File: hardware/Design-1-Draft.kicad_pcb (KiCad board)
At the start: 2 copper layers, 125 x 180 mm, 37 parts, among them J1 Barrel_Jack_Switch, M1 WATERPUMP-1, M2 WATERPUMP-2, Q1 IRLZ44N, Q2 IRLZ44N, Q3 PN2222A, SW1 Button, U3 ADS1115, U5 Tang_Nano_9K

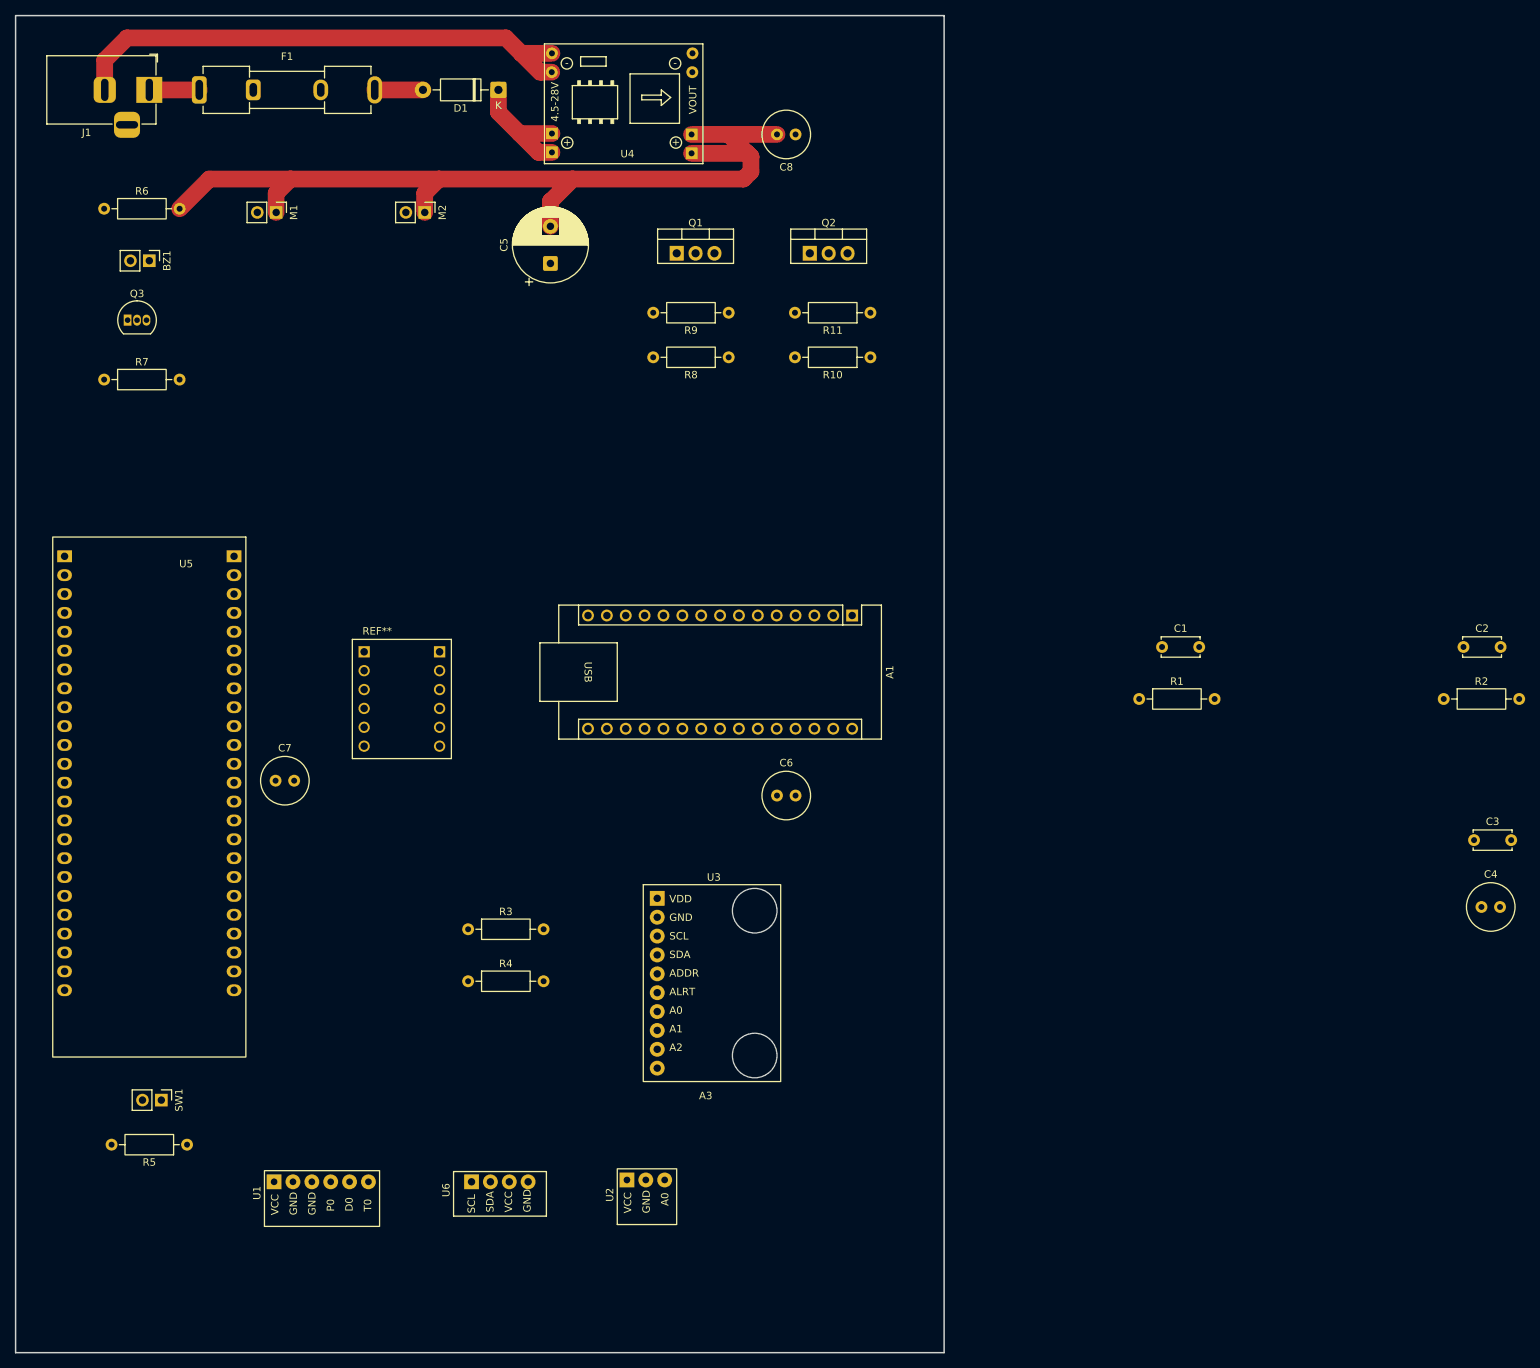
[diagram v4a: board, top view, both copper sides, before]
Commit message: updated schem (added multiple caps & 2 flyback diodes @pumps)
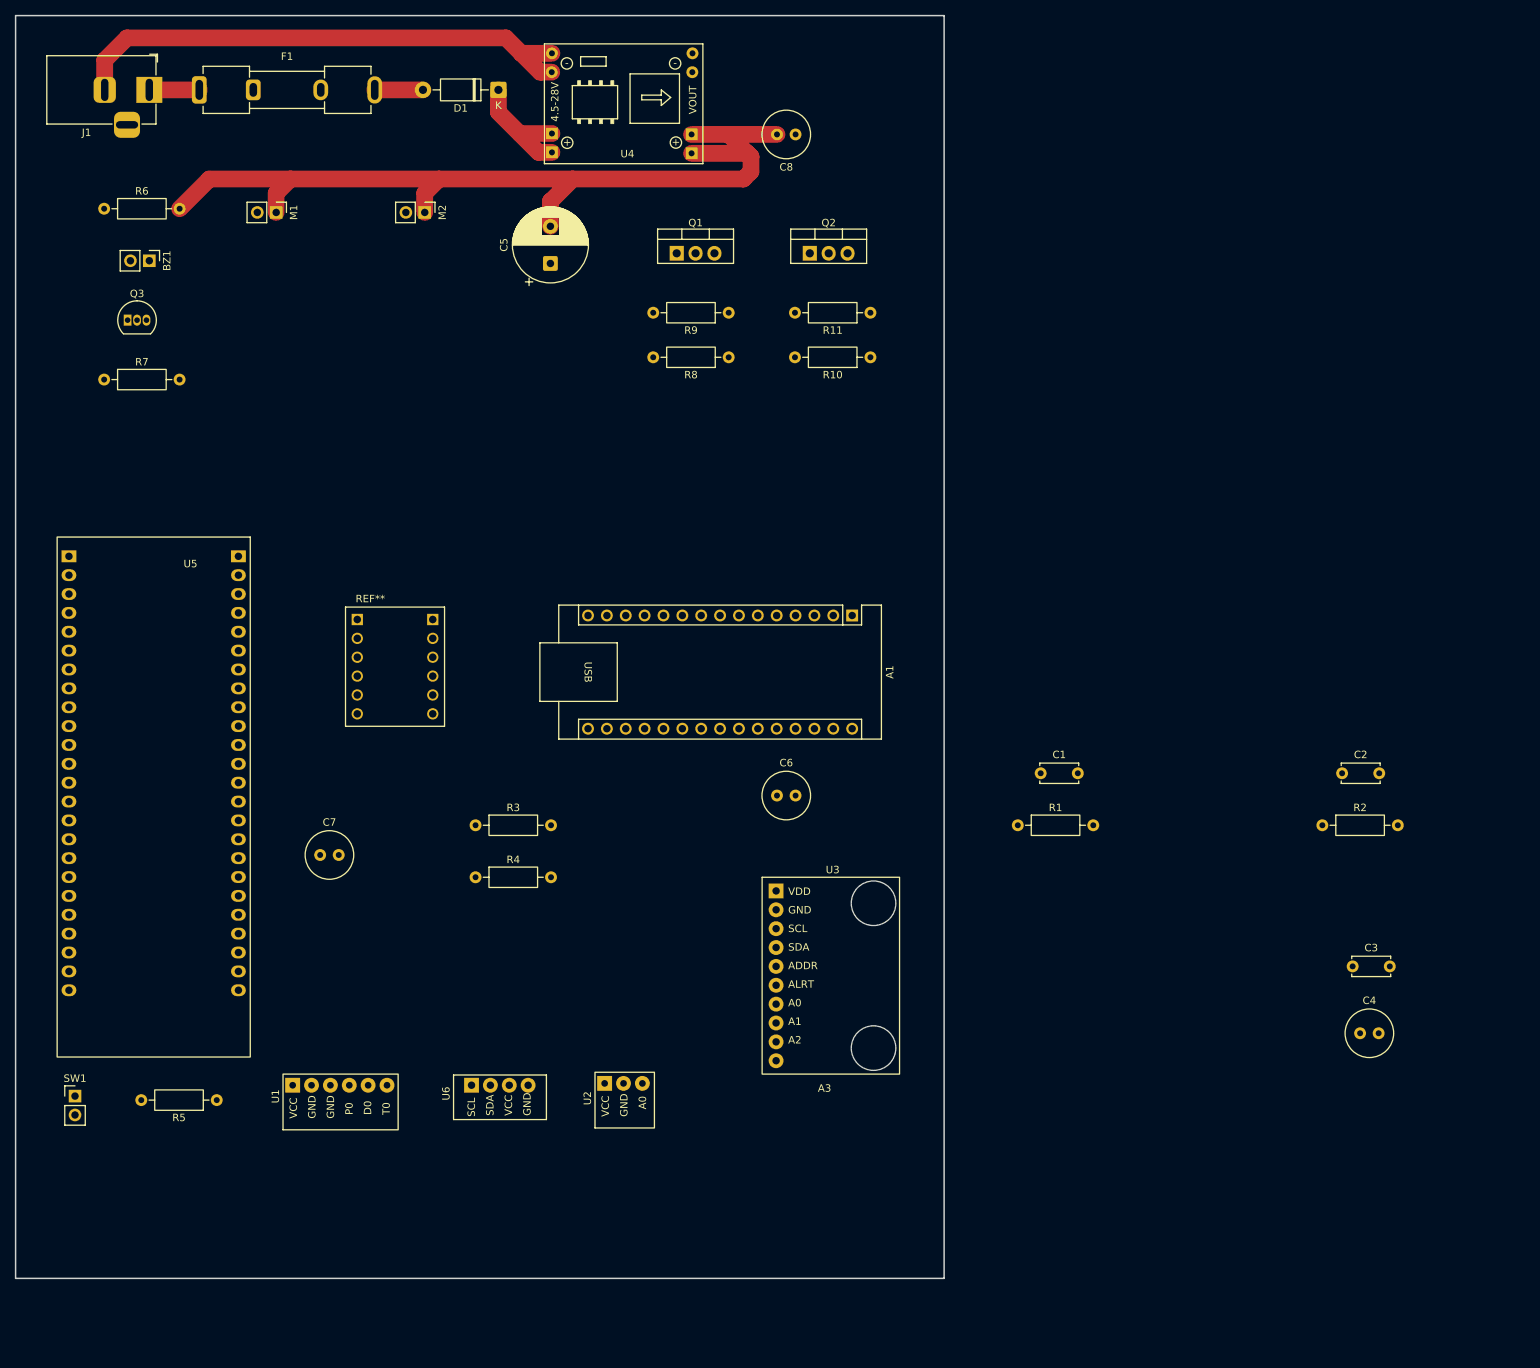
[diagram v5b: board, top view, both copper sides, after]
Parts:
- moved C1 23.6 mm to (162.0, 117.0)
- moved C3 23.6 mm to (204.0, 143.0)
- moved C4 23.6 mm to (205.0, 152.0)
- moved R1 23.6 mm to (158.9, 124.0)
- moved R2 23.6 mm to (199.9, 124.0)
- moved C2 23.6 mm to (202.6, 117.0)
- moved U3 16.0 mm to (134.0, 143.0)
- moved R3 14.0 mm to (85.9, 124.0)
- moved R4 14.0 mm to (85.9, 131.0)
- moved U2 13.3 mm to (106.0, 161.0)
- moved U1 13.2 mm to (67.5, 161.0)
- moved U6 13.0 mm to (89.2, 160.5)
- moved C7 11.7 mm to (65.0, 128.0)
- moved SW1 11.6 mm to (32.0, 160.5), turned to 0 degrees
- moved R5 7.21 mm to (51.1, 161.0)
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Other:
- board size 125 x 180 mm -> 125 x 170 mm
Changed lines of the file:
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@@
 	(footprint "Resistor_THT:R_Axial_DIN0207_L6.3mm_D2.5mm_P10.16mm_Horizontal"
 		(layer "F.Cu")
-		(at 84.92 145)
+		(at 85.92 131)
 		(descr "Resistor, Axial_DIN0207 series, Axial, Horizontal, pin pitch=10.16mm, 0.25W = 1/4W, length*diameter=6.3*2.5mm^2, http://cdn-reichelt.de/documents/datenblatt/B400/1_4W%23YAG.pdf")
 		(tags "Resistor Axial_DIN0207 series Axial Horizontal pin pitch 10.16mm 0.25W = 1/4W length 6.3mm diameter 2.5mm")
@@
 	(footprint "Resistor_THT:R_Axial_DIN0207_L6.3mm_D2.5mm_P10.16mm_Horizontal"
 		(layer "F.Cu")
-		(at 84.92 138)
+		(at 85.92 124)
 		(descr "Resistor, Axial_DIN0207 series, Axial, Horizontal, pin pitch=10.16mm, 0.25W = 1/4W, length*diameter=6.3*2.5mm^2, http://cdn-reichelt.de/documents/datenblatt/B400/1_4W%23YAG.pdf")
 		(tags "Resistor Axial_DIN0207 series Axial Horizontal pin pitch 10.16mm 0.25W = 1/4W length 6.3mm diameter 2.5mm")
@@
 	(footprint "Capacitor_THT:C_Radial_D6.3mm_H5.0mm_P2.50mm"
 		(layer "F.Cu")
-		(at 221.34 135)
+		(at 205 152)
 		(descr "C, Radial series, Radial, pin pitch=2.50mm, diameter=6.3mm, height=5mm, Non-Polar Electrolytic Capacitor")
 		(tags "C Radial series Radial pin pitch 2.50mm diameter 6.3mm height 5mm Non-Polar Electrolytic Capacitor")
@@
 	(footprint "1_CustomFootprints:TDS-ANALOG-SENSOR"
 		(layer "F.Cu")
-		(at 109 174 90)
+		(at 106 161 90)
 		(property "Reference" "U2"
 			(at 0.25 -5 90)
@@
 	(footprint "Resistor_THT:R_Axial_DIN0207_L6.3mm_D2.5mm_P10.16mm_Horizontal"
 		(layer "F.Cu")
-		(at 216.26 107)
+		(at 199.92 124)
 		(descr "Resistor, Axial_DIN0207 series, Axial, Horizontal, pin pitch=10.16mm, 0.25W = 1/4W, length*diameter=6.3*2.5mm^2, http://cdn-reichelt.de/documents/datenblatt/B400/1_4W%23YAG.pdf")
 		(tags "Resistor Axial_DIN0207 series Axial Horizontal pin pitch 10.16mm 0.25W = 1/4W length 6.3mm diameter 2.5mm")
@@
 	(footprint "1_CustomFootprints:CONV_BOB-12009"
 		(layer "F.Cu")
-		(at 76 107)
+		(at 75.08 102.65)
 		(property "Reference" "REF**"
 			(at -3.325 -9.135 0)
@@
 	(footprint "1_CustomFootprints:PH-4502C"
 		(layer "F.Cu")
-		(at 65 174 90)
+		(at 67.5 161 90)
 		(property "Reference" "U1"
 			(at 0.5 -8.5 90)
@@
 	(footprint "1_CustomFootprints:ADS1115"
 		(layer "F.Cu")
-		(at 118 144)
+		(at 134 143)
 		(property "Reference" "U3"
 			(at 0 -13 0)
@@
 	(footprint "Capacitor_THT:C_Disc_D5.0mm_W2.5mm_P5.00mm"
 		(layer "F.Cu")
-		(at 178.34 100)
+		(at 162 117)
 		(descr "C, Disc series, Radial, pin pitch=5.00mm, diameter*width=5*2.5mm^2, Capacitor, http://cdn-reichelt.de/documents/datenblatt/B300/DS_KERKO_TC.pdf")
 		(tags "C Disc series Radial pin pitch 5.00mm diameter 5mm width 2.5mm Capacitor")
@@
 	(footprint "Capacitor_THT:C_Radial_D6.3mm_H5.0mm_P2.50mm"
 		(layer "F.Cu")
-		(at 59 118)
+		(at 65 128)
 		(descr "C, Radial series, Radial, pin pitch=2.50mm, diameter=6.3mm, height=5mm, Non-Polar Electrolytic Capacitor")
 		(tags "C Radial series Radial pin pitch 2.50mm diameter 6.3mm height 5mm Non-Polar Electrolytic Capacitor")
@@
 	(footprint "Connector_PinHeader_2.54mm:PinHeader_1x02_P2.54mm_Vertical"
 		(layer "F.Cu")
-		(at 43.62 161 -90)
+		(at 32 160.46)
 		(descr "Through hole straight pin header, 1x02, 2.54mm pitch, single row")
 		(tags "Through hole pin header THT 1x02 2.54mm single row")
 		(property "Reference" "SW1"
-			(at 0 -2.38 90)
+			(at 0 -2.38 0)
 			(layer "F.SilkS")
 			(effects
@@
 		)
 		(property "Value" "Button"
-			(at 0 4.92 90)
+			(at 0 4.92 0)
 			(layer "F.Fab")
 			(effects
@@
 		)
 		(property "Datasheet" "~"
-			(at 0 0 90)
+			(at 0 0 0)
 			(layer "F.Fab")
 			(hide yes)
@@
 		)
 		(property "Description" "Push button switch, generic, two pins"
-			(at 0 0 90)
+			(at 0 0 0)
 			(layer "F.Fab")
 			(hide yes)
@@
 		(attr through_hole)
 		(fp_line
-			(start -1.38 3.92)
-			(end 1.38 3.92)
+			(start -1.38 -1.38)
+			(end 0 -1.38)
 			(stroke
 				(width 0.12)
@@
 		)
 		(fp_line
-			(start -1.38 1.27)
-			(end -1.38 3.92)
+			(start -1.38 0)
+			(end -1.38 -1.38)
 			(stroke
 				(width 0.12)
@@
 		(fp_line
 			(start -1.38 1.27)
-			(end 1.38 1.27)
+			(end -1.38 3.92)
 			(stroke
 				(width 0.12)
@@
 		)
 		(fp_line
-			(start 1.38 1.27)
-			(end 1.38 3.92)
+			(start -1.38 1.27)
+			(end 1.38 1.27)
 			(stroke
 				(width 0.12)
@@
 		)
 		(fp_line
-			(start -1.38 0)
-			(end -1.38 -1.38)
+			(start -1.38 3.92)
+			(end 1.38 3.92)
 			(stroke
 				(width 0.12)
@@
 		)
 		(fp_line
-			(start -1.38 -1.38)
-			(end 0 -1.38)
+			(start 1.38 1.27)
+			(end 1.38 3.92)
 			(stroke
 				(width 0.12)
@@
 		)
 		(fp_line
-			(start -1.77 4.32)
-			(end 1.77 4.32)
+			(start -1.77 -1.77)
+			(end -1.77 4.32)
 			(stroke
 				(width 0.05)
@@
 		)
 		(fp_line
-			(start 1.77 4.32)
-			(end 1.77 -1.77)
+			(start -1.77 4.32)
+			(end 1.77 4.32)
 			(stroke
 				(width 0.05)
@@
 		)
 		(fp_line
-			(start -1.77 -1.77)
-			(end -1.77 4.32)
+			(start 1.77 -1.77)
+			(end -1.77 -1.77)
 			(stroke
 				(width 0.05)
@@
 		)
 		(fp_line
-			(start 1.77 -1.77)
-			(end -1.77 -1.77)
+			(start 1.77 4.32)
+			(end 1.77 -1.77)
 			(stroke
 				(width 0.05)
@@
 		)
 		(fp_line
-			(start -1.27 3.81)
-			(end -1.27 -0.635)
+			(start -1.27 -0.635)
+			(end -0.635 -1.27)
 			(stroke
 				(width 0.1)
@@
 		)
 		(fp_line
-			(start 1.27 3.81)
-			(end -1.27 3.81)
+			(start -1.27 3.81)
+			(end -1.27 -0.635)
 			(stroke
 				(width 0.1)
@@
 		)
 		(fp_line
-			(start -1.27 -0.635)
-			(end -0.635 -1.27)
+			(start -0.635 -1.27)
+			(end 1.27 -1.27)
 			(stroke
 				(width 0.1)
@@
 		)
 		(fp_line
-			(start -0.635 -1.27)
-			(end 1.27 -1.27)
+			(start 1.27 -1.27)
+			(end 1.27 3.81)
 			(stroke
 				(width 0.1)
@@
 		)
 		(fp_line
-			(start 1.27 -1.27)
-			(end 1.27 3.81)
+			(start 1.27 3.81)
+			(end -1.27 3.81)
 			(stroke
 				(width 0.1)
@@
 		)
 		(fp_text user "${REFERENCE}"
-			(at 0 1.27 0)
+			(at 0 1.27 90)
 			(layer "F.Fab")
 			(effects
@@
 		)
 		(pad "1" thru_hole rect
-			(at 0 0 270)
+			(at 0 0)
 			(size 1.7 1.7)
 			(drill 1)
@@
 		)
 		(pad "2" thru_hole circle
-			(at 0 2.54 270)
+			(at 0 2.54)
 			(size 1.7 1.7)
 			(drill 1)
@@
 	(footprint "Capacitor_THT:C_Disc_D5.0mm_W2.5mm_P5.00mm"
 		(layer "F.Cu")
-		(at 220.34 126)
+		(at 204 143)
 		(descr "C, Disc series, Radial, pin pitch=5.00mm, diameter*width=5*2.5mm^2, Capacitor, http://cdn-reichelt.de/documents/datenblatt/B300/DS_KERKO_TC.pdf")
 		(tags "C Disc series Radial pin pitch 5.00mm diameter 5mm width 2.5mm Capacitor")
@@
 	(footprint "Resistor_THT:R_Axial_DIN0207_L6.3mm_D2.5mm_P10.16mm_Horizontal"
 		(layer "F.Cu")
-		(at 47.08 167 180)
+		(at 51.08 161 180)
 		(descr "Resistor, Axial_DIN0207 series, Axial, Horizontal, pin pitch=10.16mm, 0.25W = 1/4W, length*diameter=6.3*2.5mm^2, http://cdn-reichelt.de/documents/datenblatt/B400/1_4W%23YAG.pdf")
 		(tags "Resistor Axial_DIN0207 series Axial Horizontal pin pitch 10.16mm 0.25W = 1/4W length 6.3mm diameter 2.5mm")
@@
 	(footprint "0my_project:DIP-48_TangNano9K"
 		(layer "F.Cu")
-		(at 42 117 -90)
+		(at 42.59155 117 -90)
 		(property "Reference" "U5"
 			(at -28.194 -4.953 0)
@@
 	(footprint "Capacitor_THT:C_Disc_D5.0mm_W2.5mm_P5.00mm"
 		(layer "F.Cu")
-		(at 218.92 100)
+		(at 202.58 117)
 		(descr "C, Disc series, Radial, pin pitch=5.00mm, diameter*width=5*2.5mm^2, Capacitor, http://cdn-reichelt.de/documents/datenblatt/B300/DS_KERKO_TC.pdf")
 		(tags "C Disc series Radial pin pitch 5.00mm diameter 5mm width 2.5mm Capacitor")
@@
 	(footprint "1_CustomFootprints:I2C-BACKPACK-LCD"
 		(layer "F.Cu")
-		(at 89.21 173.5 90)
+		(at 89.21 160.5 90)
 		(property "Reference" "U6"
 			(at 0.38 -7.25 90)
@@
 	(footprint "Resistor_THT:R_Axial_DIN0207_L6.3mm_D2.5mm_P10.16mm_Horizontal"
 		(layer "F.Cu")
-		(at 175.26 107)
+		(at 158.92 124)
 		(descr "Resistor, Axial_DIN0207 series, Axial, Horizontal, pin pitch=10.16mm, 0.25W = 1/4W, length*diameter=6.3*2.5mm^2, http://cdn-reichelt.de/documents/datenblatt/B400/1_4W%23YAG.pdf")
 		(tags "Resistor Axial_DIN0207 series Axial Horizontal pin pitch 10.16mm 0.25W = 1/4W length 6.3mm diameter 2.5mm")
@@
 	(gr_rect
 		(start 24 15)
-		(end 149 195)
+		(end 149 185)
 		(stroke
 			(width 0.2)

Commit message: Add files via upload
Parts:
- added C10: 0.1u, Capacitor_THT:C_Disc_D5.0mm_W2.5mm_P5.00mm, F.Cu at (83.8, 62.0)
- added C11: 0.1u, Capacitor_THT:C_Disc_D5.0mm_W2.5mm_P5.00mm, F.Cu at (-39.9, 97.5)
- added C12: 0.1u, Capacitor_THT:C_Disc_D5.0mm_W2.5mm_P5.00mm, F.Cu at (135.3, 41.6)
- added C13: 0.1u, Capacitor_THT:C_Disc_D5.0mm_W2.5mm_P5.00mm, F.Cu at (177.0, 66.0)
- added C14: 0.1u, Capacitor_THT:C_Disc_D5.0mm_W2.5mm_P5.00mm, F.Cu at (163.6, 99.5)
- added C15: 0.01u, Capacitor_THT:C_Disc_D5.0mm_W2.5mm_P5.00mm, F.Cu at (185.5, 67.0)
- added C16: 0.01u, Capacitor_THT:C_Disc_D5.0mm_W2.5mm_P5.00mm, F.Cu at (175.0, 74.0)
- added C17: 0.1u, Capacitor_THT:C_Disc_D5.0mm_W2.5mm_P5.00mm, F.Cu at (186.5, 73.0)
- added C18: 0.1u, Capacitor_THT:C_Disc_D5.0mm_W2.5mm_P5.00mm, F.Cu at (176.0, 81.0)
- added C19: 0.1u, Capacitor_THT:C_Disc_D5.0mm_W2.5mm_P5.00mm, F.Cu at (185.5, 82.0)
- added C20: 100u, Capacitor_THT:C_Radial_D6.3mm_H5.0mm_P2.50mm, F.Cu at (126.8, 27.6)
- added C21: 0.1u, Capacitor_THT:C_Disc_D5.0mm_W2.5mm_P5.00mm, F.Cu at (137.3, 29.6)
- added C9: 0.1u, Capacitor_THT:C_Disc_D5.0mm_W2.5mm_P5.00mm, F.Cu at (52.4, 59.5)
- added D2: 1N5819, Diode_THT:D_DO-41_SOD81_P10.16mm_Horizontal, F.Cu at (55.4, 52.5)
- added D3: 1N5819, Diode_THT:D_DO-41_SOD81_P10.16mm_Horizontal, F.Cu at (86.4, 54.5)
- added R3: 100, Resistor_THT:R_Axial_DIN0207_L6.3mm_D2.5mm_P10.16mm_Horizontal, F.Cu at (171.4, 106.0)
- M1: value WATERPUMP-1 -> WP-1
- M2: value WATERPUMP-2 -> WP-2
- moved Q3 97.5 mm to (-44.3, 106.5)
- moved R7 97.5 mm to (-47.5, 114.5)
- moved BZ1 94.1 mm to (-41.4, 91.5)
- moved R8 91.3 mm to (28.8, 56.0), turned to 0 degrees
- moved R6 83.4 mm to (103.4, 90.0)
- moved R9 81.3 mm to (39.1, 63.0)
- moved R11 79.3 mm to (60.2, 63.0), turned to 0 degrees
- moved R10 78.9 mm to (60.4, 56.0), turned to 0 degrees
- moved Q1 76.6 mm to (36.4, 46.5), turned to 180 degrees
- moved Q2 62.3 mm to (68.6, 47.5), turned to 180 degrees
- moved U5 13.6 mm to (37.4, 129.6)
- moved R5 13.2 mm to (53.6, 174.0)
- moved SW1 13.2 mm to (34.5, 173.5)
- moved U1 13.2 mm to (70.0, 174.0)
- moved U2 13.2 mm to (108.5, 174.0)
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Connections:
- C5 pad 2: Net-(A1-VIN) -> Net-(D2-K)
- C8 pad 2: Net-(A1-VIN) -> Net-(D2-K)
- J1 pad 2: Net-(U4-IN-) -> Net-(J1-Pad2)
- M1 pad 1: Net-(A1-VIN) -> Net-(D2-K)
- M2 pad 1: Net-(A1-VIN) -> Net-(D2-K)
- R11 pad 1: Net-(Q2-G) -> GND
- R11 pad 2: GND -> Net-(Q2-G)
- R5 pad 2: Net-(U5-69_IOT42A) -> Net-(R3-Pad1)
- R6 pad 2: Net-(A1-VIN) -> Net-(Q3-B)
- R9 pad 1: GND -> Net-(Q1-G)
- R9 pad 2: Net-(Q1-G) -> GND
- SW1 pad 2: Net-(U5-69_IOT42A) -> Net-(R3-Pad1)
- U4 pad 2: Net-(U4-IN-) -> Net-(D1-K)
- U4 pad 3: Net-(A1-VIN) -> Net-(J1-Pad2)
- U4 pad 4: GND -> Net-(J1-Pad2)
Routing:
- net Net-(D2-K): track 0.00 -> 161.4 mm
- net Net-(A1-VIN): track 123.1 -> 26.5 mm
- net Net-(U4-IN-): track 71.5 -> 0.00 mm
- net Net-(J1-Pad2): track 0.00 -> 71.5 mm
- net Net-(D2-A): track 0.00 -> 34.5 mm
- net Net-(D3-A): track 0.00 -> 34.4 mm
- net Net-(Q1-G): track 0.00 -> 25.4 mm
- net Net-(Q2-G): track 0.00 -> 23.7 mm
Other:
- board size 125 x 170 mm -> 130 x 170 mm
